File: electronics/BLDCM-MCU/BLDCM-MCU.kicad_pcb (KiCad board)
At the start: 4 copper layers, 32 x 32 mm, 91 parts, among them J1 52991-0308, K1 EVPAKE31A, U1 STM32F446RE, U10 SK6805, U11 SK6805, U12 SK6805, U13 SK6805, U14 SK6805, U15 SK6805, U16 SK6805, U17 SK6805, U18 SK6805, U19 SK6805, U2 SN74LV1T34DBVR, U20 AS5048A, U3 ISM330DHCX, U4 SK6805, U5 SK6805, U6 SK6805, U7 SK6805, U8 SK6805, U9 SK6805, Y1 ECS-3225MVLC-240-CN

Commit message: Feat: Setup KiCad project specific libraries
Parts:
- C6: footprint BrenoCQ:C_0603 -> BrenoCQ:C_0402
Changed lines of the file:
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@@
 		)
 	)
-	(footprint "BrenoCQ:C_0603"
+	(footprint "BrenoCQ:C_0402"
 		(layer "B.Cu")
 		(at 144.7999 93.2002 -45)
@@
 			(unlocked yes)
 			(layer "B.SilkS")
-			(hide yes)
 			(effects
 				(font
@@
 		(attr smd)
 		(fp_line
-			(start -0.146267 0.51)
-			(end 0.146267 0.51)
+			(start -0.100201 0.36)
+			(end 0.100201 0.36)
 			(stroke
 				(width 0.12)
@@
 		)
 		(fp_line
-			(start -0.146267 -0.51)
-			(end 0.146267 -0.51)
+			(start -0.100201 -0.36)
+			(end 0.100201 -0.36)
 			(stroke
 				(width 0.12)
@@
 		)
 		(fp_line
-			(start -1.65 0.73)
-			(end 1.65 0.73)
+			(start -1.11 0.47)
+			(end 1.11 0.47)
 			(stroke
 				(width 0.05)
@@
 		)
 		(fp_line
-			(start -1.65 -0.73)
-			(end -1.65 0.73)
+			(start -1.11 -0.47)
+			(end -1.11 0.47)
 			(stroke
 				(width 0.05)
@@
 		)
 		(fp_line
-			(start 1.65 0.73)
-			(end 1.65 -0.73)
+			(start 1.11 0.47)
+			(end 1.11 -0.47)
 			(stroke
 				(width 0.05)
@@
 		)
 		(fp_line
-			(start 1.65 -0.73)
-			(end -1.65 -0.73)
+			(start 1.11 -0.47)
+			(end -1.11 -0.47)
 			(stroke
 				(width 0.05)
@@
 		)
 		(fp_line
-			(start -0.8 0.4)
-			(end 0.8 0.4)
+			(start -0.5 0.25)
+			(end 0.5 0.25)
 			(stroke
 				(width 0.1)
@@
 		)
 		(fp_line
-			(start -0.8 -0.4)
-			(end -0.8 0.4)
+			(start -0.5 -0.25)
+			(end -0.5 0.25)
 			(stroke
 				(width 0.1)
@@
 		)
 		(fp_line
-			(start 0.8 0.4)
-			(end 0.8 -0.4)
+			(start 0.5 0.25)
+			(end 0.5 -0.25)
 			(stroke
 				(width 0.1)
@@
 		)
 		(fp_line
-			(start 0.8 -0.4)
-			(end -0.8 -0.4)
+			(start 0.5 -0.25)
+			(end -0.5 -0.25)
 			(stroke
 				(width 0.1)
@@
 		)
 		(pad "1" smd roundrect
-			(at -0.862501 0 315)
-			(size 1.075 0.95)
+			(at -0.572501 0 315)
+			(size 0.765 0.64)
 			(layers "B.Cu" "B.Mask" "B.Paste")
 			(roundrect_rratio 0.25)
@@
 		)
 		(pad "2" smd roundrect
-			(at 0.862501 0 315)
-			(size 1.075 0.95)
+			(at 0.572501 0 315)
+			(size 0.765 0.64)
 			(layers "B.Cu" "B.Mask" "B.Paste")
 			(roundrect_rratio 0.25)
@@
 		)
 		(embedded_fonts no)
-		(model "${BRENOCQ_DIR}/BrenoCQ.3dshapes/C_0603.step"
+		(model "../BrenoCQ.3dshapes/C_0402.step"
 			(offset
 				(xyz 0 0 0)

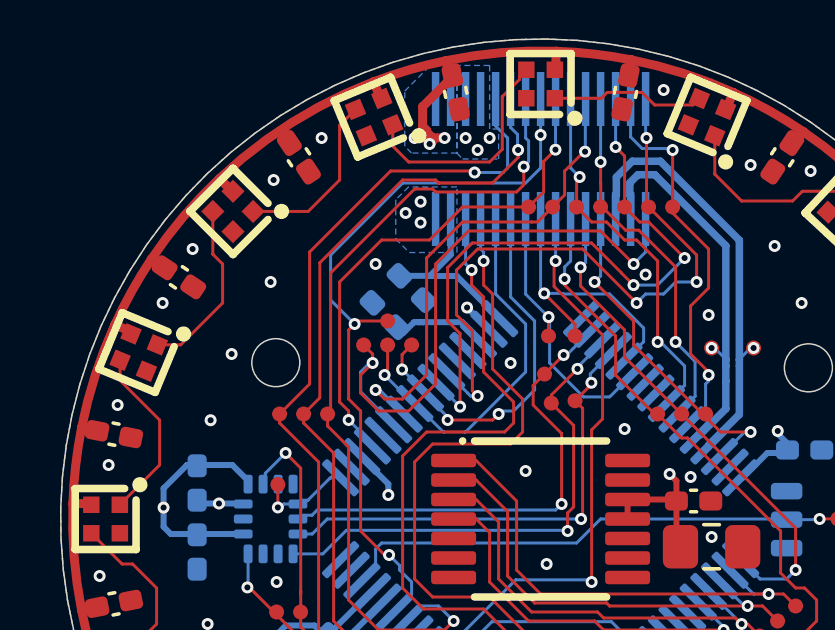
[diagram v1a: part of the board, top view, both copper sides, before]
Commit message: Fix: PCB 3D model references
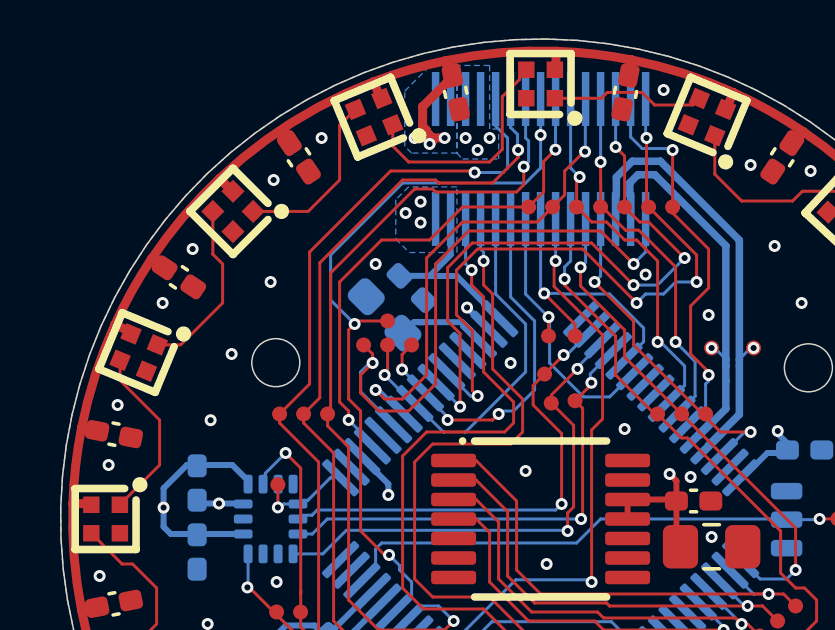
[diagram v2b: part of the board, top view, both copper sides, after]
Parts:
- C6: footprint BrenoCQ:C_0402 -> BrenoCQ:C_0603
